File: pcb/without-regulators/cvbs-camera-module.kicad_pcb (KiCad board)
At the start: 4 copper layers, 35 x 33 mm, 13 parts, among them J1 X.FL-PR-SMT1-2(80), J2 5052740612, J3 X.FL-R-SMT-1(02), J5 Conn_01x03, J6 X.FL-R-SMT-1(02), U1 cvbs-camera

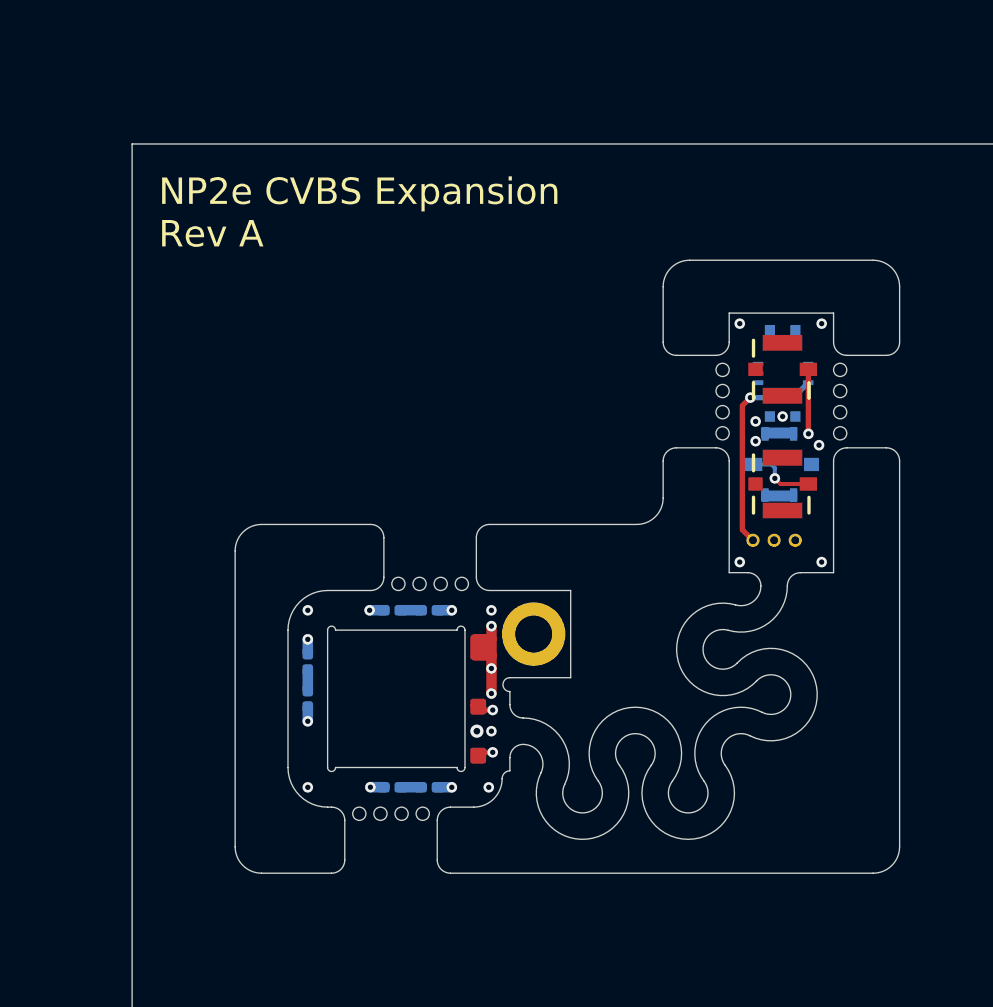
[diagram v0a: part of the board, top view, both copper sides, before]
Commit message: Address feedback
- Fill out title blocks
- LEDs 0201 -> 0402 & assign PN
- Power LEDs with 2.85V regulator
- Remove noise on fab layers
- Thicken flex cable
- Add .sldprt & .dxf files for flex pattern
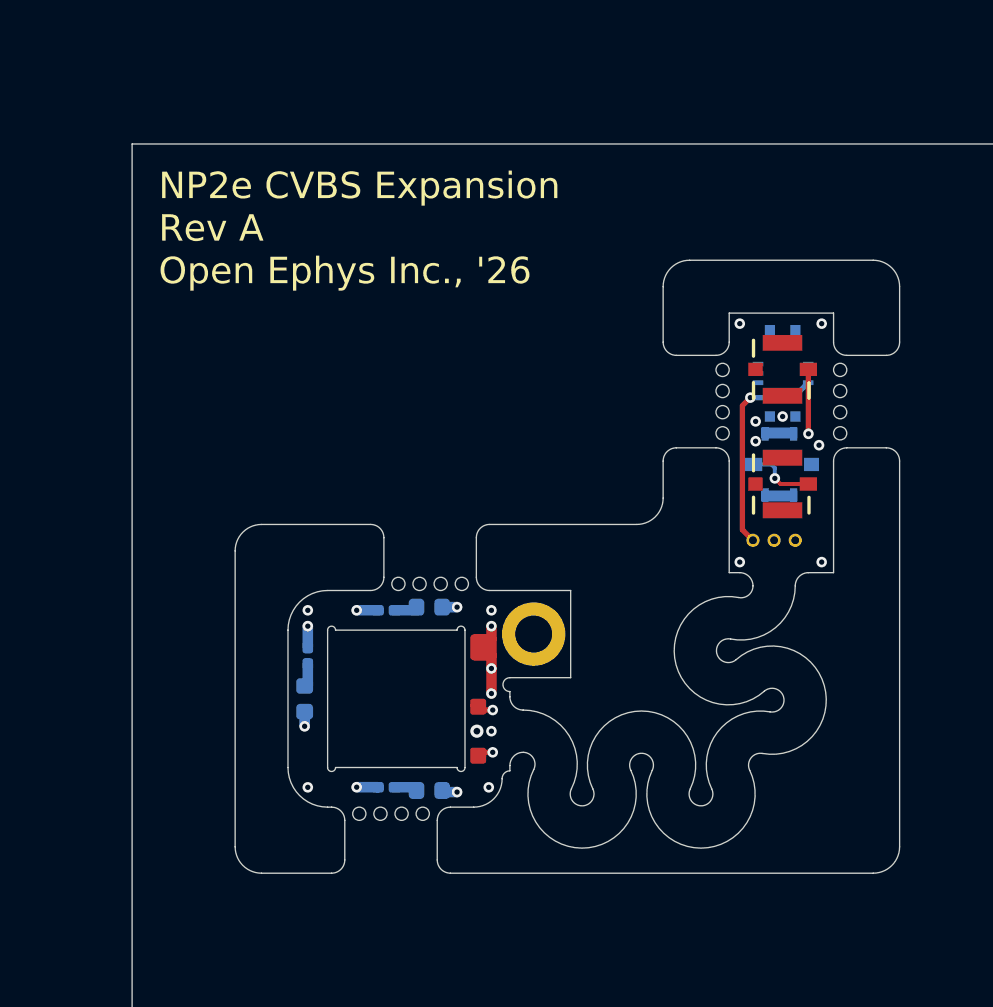
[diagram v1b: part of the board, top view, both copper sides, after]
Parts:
- D1, D2, D3: value LED -> IN-S42CTQIR; footprint LED_SMD:LED_0201_0603Metric -> LED_SMD:LED_0402_1005Metric
- moved R1 0.23 mm to (96.7, 68.4)
- moved R2 0.22 mm to (99.6, 66.7)
- moved R3 0.22 mm to (99.6, 73.3)
- moved D1 0.12 mm to (96.5, 70.0)
- moved D2 0.12 mm to (101.2, 66.5)
- moved D3 0.12 mm to (101.2, 73.5)
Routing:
- net +2V5: track 12.8 -> 13.4 mm
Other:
- outline, holes or cut-outs redrawn
- board text added: "NP2e CVBS Expansion Rev A Open Ephys Inc., '26"
- board text removed: "NP2e CVBS Expansion Rev A"
